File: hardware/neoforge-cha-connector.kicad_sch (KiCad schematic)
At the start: 1 part, among them J2 AES_CN4_CHA

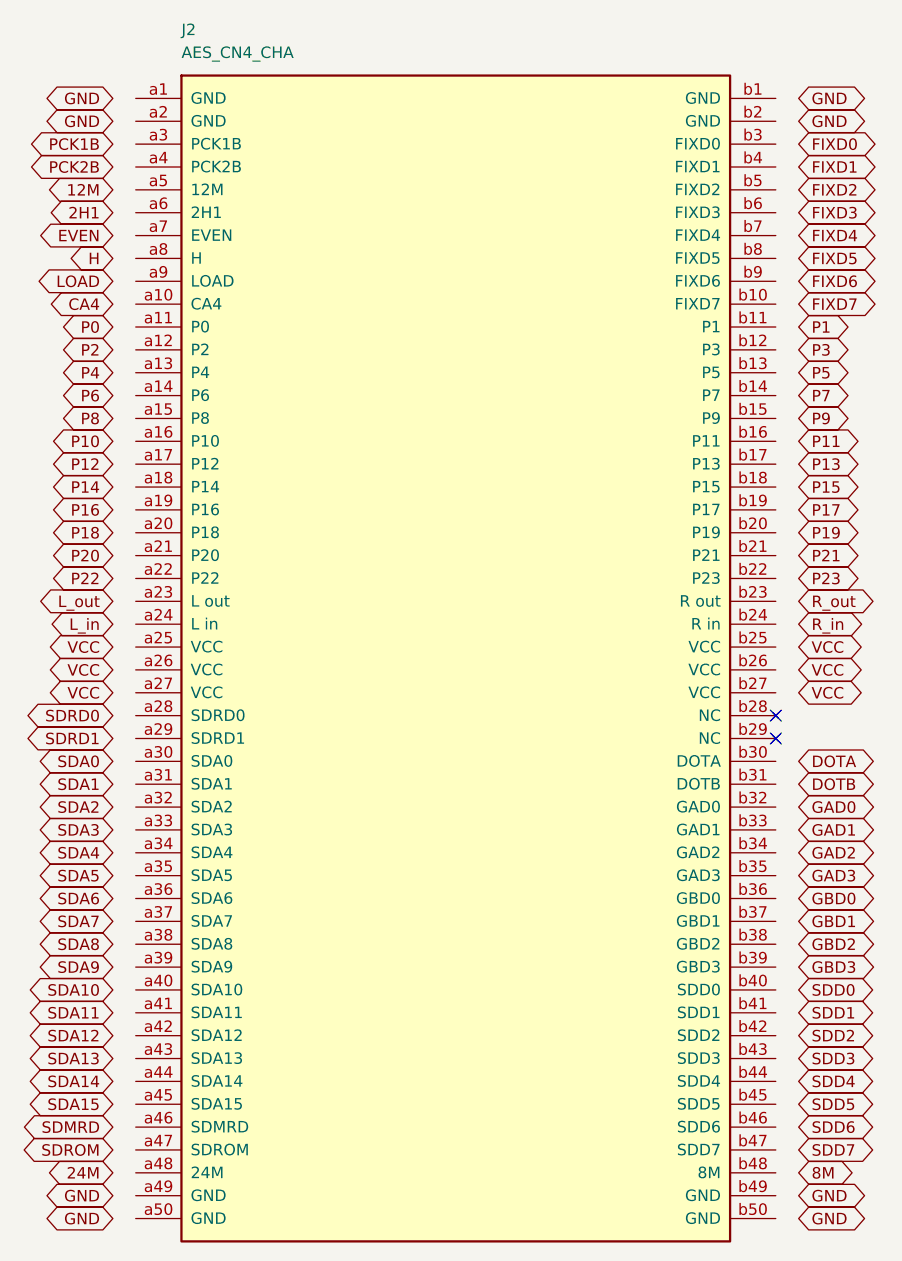
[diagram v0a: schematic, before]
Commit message: hardware: connector netlist verified 100/100
Exported from KiCad and checked back against the pinout CSV:

    J1 -> PROG CN5
      identified from the symbol's Value
      100/100 pins match the pinout
      no issues

The chain closes with nothing transcribed by hand: a CSV verified against
two independent sources, a symbol generated from it, a sheet generated
from it, KiCad's netlist exported from that, and the checker agreeing.

Three bugs were caught on the way and all three were in the tooling, not
the data - the Y-axis inversion between symbol and sheet space, an empty
lib_symbols that rendered a placeholder, and a label offset that produced
a sheet which looked correct and connected nothing. The last is the one
netcheck exists for.

Roadmap: Phase 7's connector item is electrically done, mechanically
open. The footprint still needs measuring off a real cartridge.
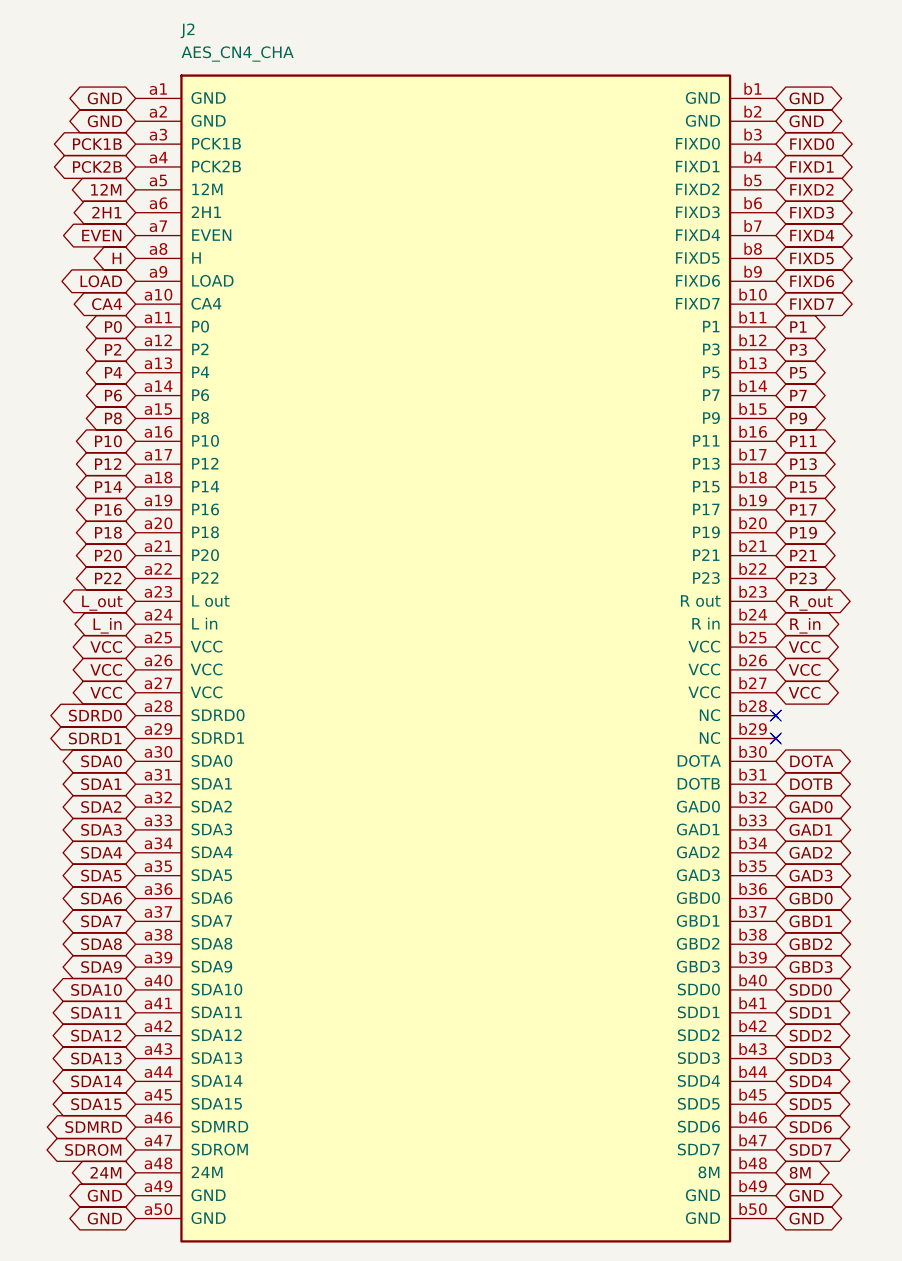
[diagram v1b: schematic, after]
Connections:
- net 12M: now also J2.a5 (12M)
- net 24M: now also J2.a48 (24M)
- net 2H1: now also J2.a6 (2H1)
- net 8M: now also J2.b48 (8M)
- net CA4: now also J2.a10 (CA4)
- net DOTA: now also J2.b30 (DOTA)
- net DOTB: now also J2.b31 (DOTB)
- net EVEN: now also J2.a7 (EVEN)
- net FIXD0: now also J2.b3 (FIXD0)
- net FIXD1: now also J2.b4 (FIXD1)
- net FIXD2: now also J2.b5 (FIXD2)
- net FIXD3: now also J2.b6 (FIXD3)
- net FIXD4: now also J2.b7 (FIXD4)
- net FIXD5: now also J2.b8 (FIXD5)
- net FIXD6: now also J2.b9 (FIXD6)
- net FIXD7: now also J2.b10 (FIXD7)
- net GAD0: now also J2.b32 (GAD0)
- net GAD1: now also J2.b33 (GAD1)
- net GAD2: now also J2.b34 (GAD2)
- net GAD3: now also J2.b35 (GAD3)
- net GBD0: now also J2.b36 (GBD0)
- net GBD1: now also J2.b37 (GBD1)
- net GBD2: now also J2.b38 (GBD2)
- net GBD3: now also J2.b39 (GBD3)
- net GND: now also J2.a1 (GND), J2.a2 (GND), J2.a49 (GND), J2.a50 (GND), J2.b1 (GND), J2.b2 (GND), J2.b49 (GND), J2.b50 (GND)
- net H: now also J2.a8 (H)
- net LOAD: now also J2.a9 (LOAD)
- net L_in: now also J2.a24 (L in)
- net L_out: now also J2.a23 (L out)
- net P0: now also J2.a11 (P0)
- net P1: now also J2.b11 (P1)
- net P10: now also J2.a16 (P10)
- net P11: now also J2.b16 (P11)
- net P12: now also J2.a17 (P12)
- net P13: now also J2.b17 (P13)
- net P14: now also J2.a18 (P14)
- net P15: now also J2.b18 (P15)
- net P16: now also J2.a19 (P16)
- net P17: now also J2.b19 (P17)
- net P18: now also J2.a20 (P18)
- net P19: now also J2.b20 (P19)
- net P2: now also J2.a12 (P2)
- net P20: now also J2.a21 (P20)
- net P21: now also J2.b21 (P21)
- net P22: now also J2.a22 (P22)
- net P23: now also J2.b22 (P23)
- net P3: now also J2.b12 (P3)
- net P4: now also J2.a13 (P4)
- net P5: now also J2.b13 (P5)
- net P6: now also J2.a14 (P6)
- net P7: now also J2.b14 (P7)
- net P8: now also J2.a15 (P8)
- net P9: now also J2.b15 (P9)
- net PCK1B: now also J2.a3 (PCK1B)
- net PCK2B: now also J2.a4 (PCK2B)
- net R_in: now also J2.b24 (R in)
- net R_out: now also J2.b23 (R out)
- net SDA0: now also J2.a30 (SDA0)
- net SDA1: now also J2.a31 (SDA1)
- net SDA10: now also J2.a40 (SDA10)
- net SDA11: now also J2.a41 (SDA11)
- net SDA12: now also J2.a42 (SDA12)
- net SDA13: now also J2.a43 (SDA13)
- net SDA14: now also J2.a44 (SDA14)
- net SDA15: now also J2.a45 (SDA15)
- net SDA2: now also J2.a32 (SDA2)
- net SDA3: now also J2.a33 (SDA3)
- net SDA4: now also J2.a34 (SDA4)
- net SDA5: now also J2.a35 (SDA5)
- net SDA6: now also J2.a36 (SDA6)
- net SDA7: now also J2.a37 (SDA7)
- net SDA8: now also J2.a38 (SDA8)
- net SDA9: now also J2.a39 (SDA9)
- net SDD0: now also J2.b40 (SDD0)
- net SDD1: now also J2.b41 (SDD1)
- net SDD2: now also J2.b42 (SDD2)
- net SDD3: now also J2.b43 (SDD3)
- net SDD4: now also J2.b44 (SDD4)
- net SDD5: now also J2.b45 (SDD5)
- net SDD6: now also J2.b46 (SDD6)
- net SDD7: now also J2.b47 (SDD7)
- net SDMRD: now also J2.a46 (SDMRD)
- net SDRD0: now also J2.a28 (SDRD0)
- net SDRD1: now also J2.a29 (SDRD1)
- net SDROM: now also J2.a47 (SDROM)
- net VCC: now also J2.a25 (VCC), J2.a26 (VCC), J2.a27 (VCC), J2.b25 (VCC), J2.b26 (VCC), J2.b27 (VCC)
